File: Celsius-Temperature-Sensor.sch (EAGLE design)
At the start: 19 parts, among them Q1 BSS138, Q2 BSS138

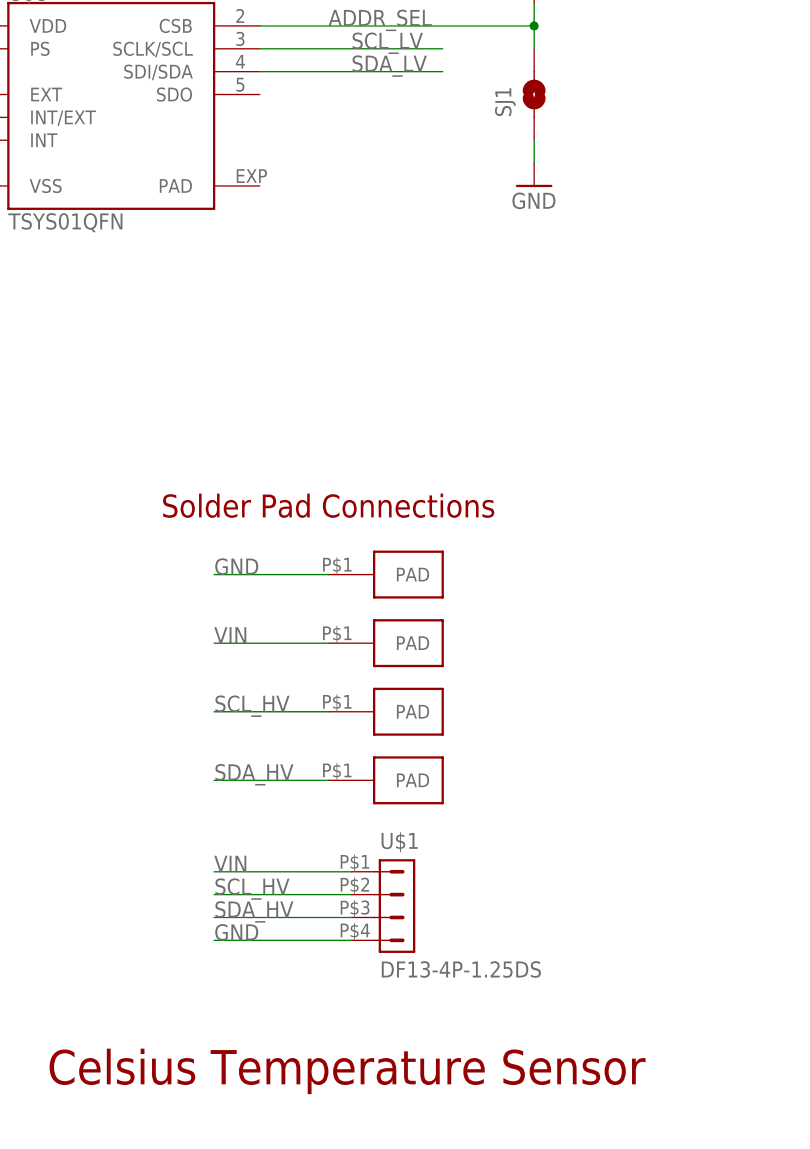
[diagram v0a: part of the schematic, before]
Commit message: Updated to new board outline. Still needs some fillets in the corners for machining.
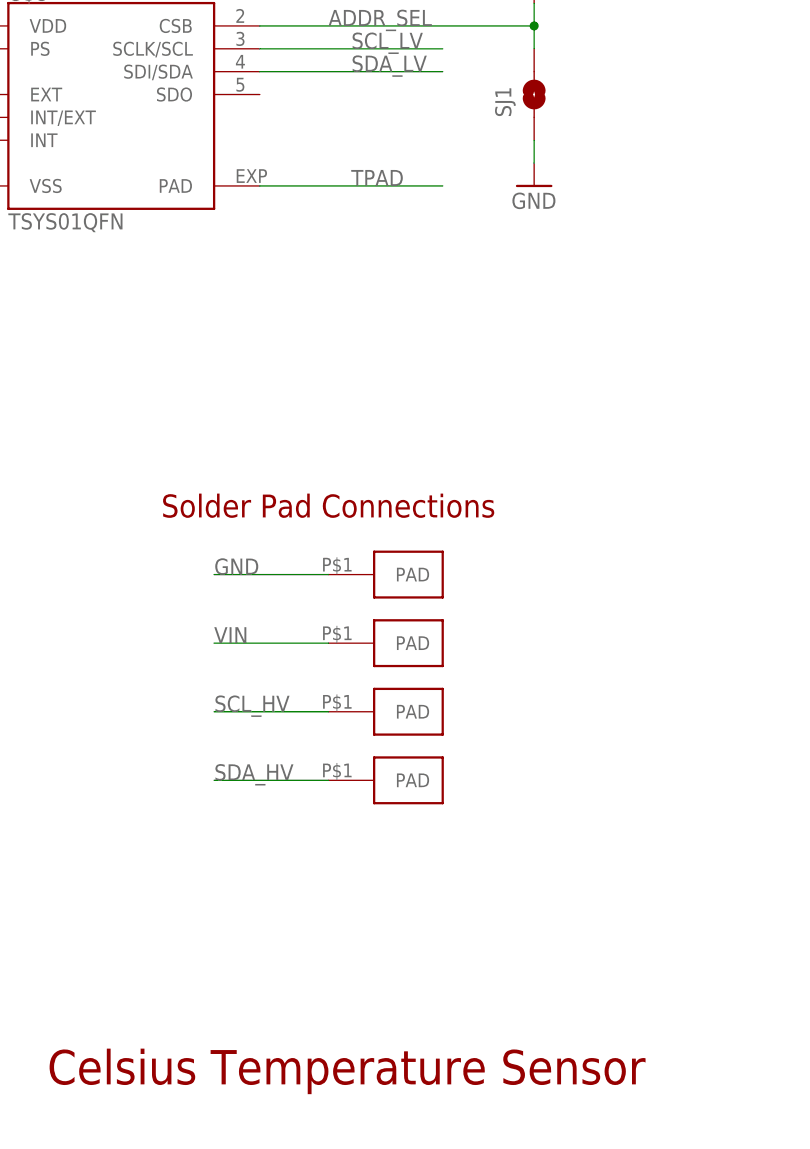
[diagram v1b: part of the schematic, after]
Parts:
- removed U$1: DF13-4P-1.25DS, con-hirose-df13:DF13-4P-1.25DS
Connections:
- new net TPAD: U$8.PAD
- net GND: no longer U$1.4
- net SCL_HV: no longer U$1.2
- net SDA_HV: no longer U$1.3
- net VIN: no longer U$1.1
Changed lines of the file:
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@@
 <grid distance="0.1" unitdist="inch" unit="inch" style="lines" multiple="1" display="no" altdistance="0.01" altunitdist="inch" altunit="inch"/>
 <layers>
-<layer number="1" name="Top" color="4" fill="1" visible="yes" active="no"/>
-<layer number="2" name="Route2" color="1" fill="3" visible="yes" active="no"/>
-<layer number="3" name="Route3" color="4" fill="3" visible="yes" active="no"/>
-<layer number="14" name="Route14" color="1" fill="6" visible="yes" active="no"/>
-<layer number="15" name="Route15" color="4" fill="6" visible="yes" active="no"/>
-<layer number="16" name="Bottom" color="1" fill="1" visible="yes" active="no"/>
-<layer number="17" name="Pads" color="2" fill="1" visible="yes" active="no"/>
-<layer number="18" name="Vias" color="2" fill="1" visible="yes" active="no"/>
-<layer number="19" name="Unrouted" color="6" fill="1" visible="yes" active="no"/>
-<layer number="20" name="Dimension" color="15" fill="1" visible="yes" active="no"/>
-<layer number="21" name="tPlace" color="7" fill="1" visible="yes" active="no"/>
-<layer number="22" name="bPlace" color="7" fill="1" visible="yes" active="no"/>
-<layer number="23" name="tOrigins" color="15" fill="1" visible="yes" active="no"/>
-<layer number="24" name="bOrigins" color="15" fill="1" visible="yes" active="no"/>
-<layer number="25" name="tNames" color="7" fill="1" visible="yes" active="no"/>
-<layer number="26" name="bNames" color="7" fill="1" visible="yes" active="no"/>
-<layer number="27" name="tValues" color="7" fill="1" visible="yes" active="no"/>
-<layer number="28" name="bValues" color="7" fill="1" visible="yes" active="no"/>
+<layer number="1" name="Top" color="4" fill="1" visible="no" active="no"/>
+<layer number="2" name="Route2" color="1" fill="3" visible="no" active="no"/>
+<layer number="3" name="Route3" color="4" fill="3" visible="no" active="no"/>
+<layer number="14" name="Route14" color="1" fill="6" visible="no" active="no"/>
+<layer number="15" name="Route15" color="4" fill="6" visible="no" active="no"/>
+<layer number="16" name="Bottom" color="1" fill="1" visible="no" active="no"/>
+<layer number="17" name="Pads" color="2" fill="1" visible="no" active="no"/>
+<layer number="18" name="Vias" color="2" fill="1" visible="no" active="no"/>
+<layer number="19" name="Unrouted" color="6" fill="1" visible="no" active="no"/>
+<layer number="20" name="Dimension" color="15" fill="1" visible="no" active="no"/>
+<layer number="21" name="tPlace" color="7" fill="1" visible="no" active="no"/>
+<layer number="22" name="bPlace" color="7" fill="1" visible="no" active="no"/>
+<layer number="23" name="tOrigins" color="15" fill="1" visible="no" active="no"/>
+<layer number="24" name="bOrigins" color="15" fill="1" visible="no" active="no"/>
+<layer number="25" name="tNames" color="7" fill="1" visible="no" active="no"/>
+<layer number="26" name="bNames" color="7" fill="1" visible="no" active="no"/>
+<layer number="27" name="tValues" color="7" fill="1" visible="no" active="no"/>
+<layer number="28" name="bValues" color="7" fill="1" visible="no" active="no"/>
 <layer number="29" name="tStop" color="7" fill="3" visible="no" active="no"/>
 <layer number="30" name="bStop" color="7" fill="6" visible="no" active="no"/>
@@
 <layer number="35" name="tGlue" color="7" fill="4" visible="no" active="no"/>
 <layer number="36" name="bGlue" color="7" fill="5" visible="no" active="no"/>
-<layer number="37" name="tTest" color="7" fill="1" visible="yes" active="no"/>
-<layer number="38" name="bTest" color="7" fill="1" visible="yes" active="no"/>
+<layer number="37" name="tTest" color="7" fill="1" visible="no" active="no"/>
+<layer number="38" name="bTest" color="7" fill="1" visible="no" active="no"/>
 <layer number="39" name="tKeepout" color="4" fill="11" visible="no" active="no"/>
 <layer number="40" name="bKeepout" color="1" fill="11" visible="no" active="no"/>
@@
 <layer number="44" name="Drills" color="7" fill="1" visible="no" active="no"/>
 <layer number="45" name="Holes" color="7" fill="1" visible="no" active="no"/>
-<layer number="46" name="Milling" color="3" fill="1" visible="yes" active="no"/>
-<layer number="47" name="Measures" color="7" fill="1" visible="yes" active="no"/>
-<layer number="48" name="Document" color="7" fill="1" visible="yes" active="no"/>
-<layer number="49" name="Reference" color="7" fill="1" visible="yes" active="no"/>
-<layer number="50" name="dxf" color="7" fill="1" visible="yes" active="no"/>
-<layer number="51" name="tDocu" color="7" fill="1" visible="yes" active="no"/>
-<layer number="52" name="bDocu" color="7" fill="1" visible="yes" active="no"/>
-<layer number="53" name="tGND_GNDA" color="7" fill="9" visible="yes" active="no"/>
-<layer number="54" name="bGND_GNDA" color="1" fill="9" visible="yes" active="no"/>
-<layer number="56" name="wert" color="7" fill="1" visible="yes" active="no"/>
-<layer number="57" name="tCAD" color="7" fill="1" visible="yes" active="no"/>
+<layer number="46" name="Milling" color="3" fill="1" visible="no" active="no"/>
+<layer number="47" name="Measures" color="7" fill="1" visible="no" active="no"/>
+<layer number="48" name="Document" color="7" fill="1" visible="no" active="no"/>
+<layer number="49" name="Reference" color="7" fill="1" visible="no" active="no"/>
+<layer number="50" name="dxf" color="7" fill="1" visible="no" active="no"/>
+<layer number="51" name="tDocu" color="7" fill="1" visible="no" active="no"/>
+<layer number="52" name="bDocu" color="7" fill="1" visible="no" active="no"/>
+<layer number="53" name="tGND_GNDA" color="7" fill="9" visible="no" active="no"/>
+<layer number="54" name="bGND_GNDA" color="1" fill="9" visible="no" active="no"/>
+<layer number="56" name="wert" color="7" fill="1" visible="no" active="no"/>
+<layer number="57" name="tCAD" color="7" fill="1" visible="no" active="no"/>
 <layer number="90" name="Modules" color="5" fill="1" visible="yes" active="yes"/>
 <layer number="91" name="Nets" color="2" fill="1" visible="yes" active="yes"/>
@@
 <part name="GND4" library="supply1" deviceset="GND" device=""/>
 <part name="R6" library="resistor" deviceset="R-US_" device="R0402" value="10K"/>
-<part name="U$1" library="con-hirose-df13" deviceset="DF13-4P-1.25" device="DS" value="DF13-4P-1.25DS"/>
 </parts>
 <sheets>
@@
 <instance part="GND4" gate="1" x="106.68" y="38.1"/>
 <instance part="R6" gate="G$1" x="106.68" y="63.5" rot="R90"/>
-<instance part="U$1" gate="G$1" x="91.44" y="-40.64"/>
 </instances>
 <busses>
@@
 <pinref part="SJ1" gate="G$1" pin="1"/>
 <wire x1="106.68" y1="40.64" x2="106.68" y2="43.18" width="0.1524" layer="91"/>
-</segment>
-<segment>
-<pinref part="U$1" gate="G$1" pin="4"/>
-<wire x1="86.36" y1="-45.72" x2="71.12" y2="-45.72" width="0.1524" layer="91"/>
-<label x="71.12" y="-45.72" size="1.778" layer="95"/>
 </segment>
 </net>
@@
 <label x="71.12" y="-27.94" size="1.778" layer="95"/>
 <pinref part="U$6" gate="G$1" pin="PAD"/>
-</segment>
-<segment>
-<pinref part="U$1" gate="G$1" pin="3"/>
-<wire x1="86.36" y1="-43.18" x2="71.12" y2="-43.18" width="0.1524" layer="91"/>
-<label x="71.12" y="-43.18" size="1.778" layer="95"/>
 </segment>
 </net>
@@
 <pinref part="U$5" gate="G$1" pin="PAD"/>
 </segment>
-<segment>
-<pinref part="U$1" gate="G$1" pin="2"/>
-<wire x1="86.36" y1="-40.64" x2="71.12" y2="-40.64" width="0.1524" layer="91"/>
-<label x="71.12" y="-40.64" size="1.778" layer="95"/>
-</segment>
 </net>
 <net name="VIN" class="0">
@@
 <label x="71.12" y="-12.7" size="1.778" layer="95"/>
 <pinref part="U$4" gate="G$1" pin="PAD"/>
-</segment>
-<segment>
-<pinref part="U$1" gate="G$1" pin="1"/>
-<wire x1="86.36" y1="-38.1" x2="71.12" y2="-38.1" width="0.1524" layer="91"/>
-<label x="71.12" y="-38.1" size="1.778" layer="95"/>
 </segment>
 </net>
@@
 </segment>
 </net>
+<net name="TPAD" class="0">
+<segment>
+<pinref part="U$8" gate="G$1" pin="PAD"/>
+<wire x1="76.2" y1="38.1" x2="96.52" y2="38.1" width="0.1524" layer="91"/>
+<label x="86.36" y="38.1" size="1.778" layer="95"/>
+</segment>
+</net>
